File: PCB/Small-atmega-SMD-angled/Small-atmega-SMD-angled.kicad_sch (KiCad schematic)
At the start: 26 parts, among them J1 Daisy port out, J2 2-pin header, J3 ICSP_ISP6, J4 Daisy port in, K1 HYC77-TF09-200, U1 PC817C-S, U2 ATmega328P-AU, U3 SE5218, U4 TXB0104PWR, Y1 Resonator_GND2

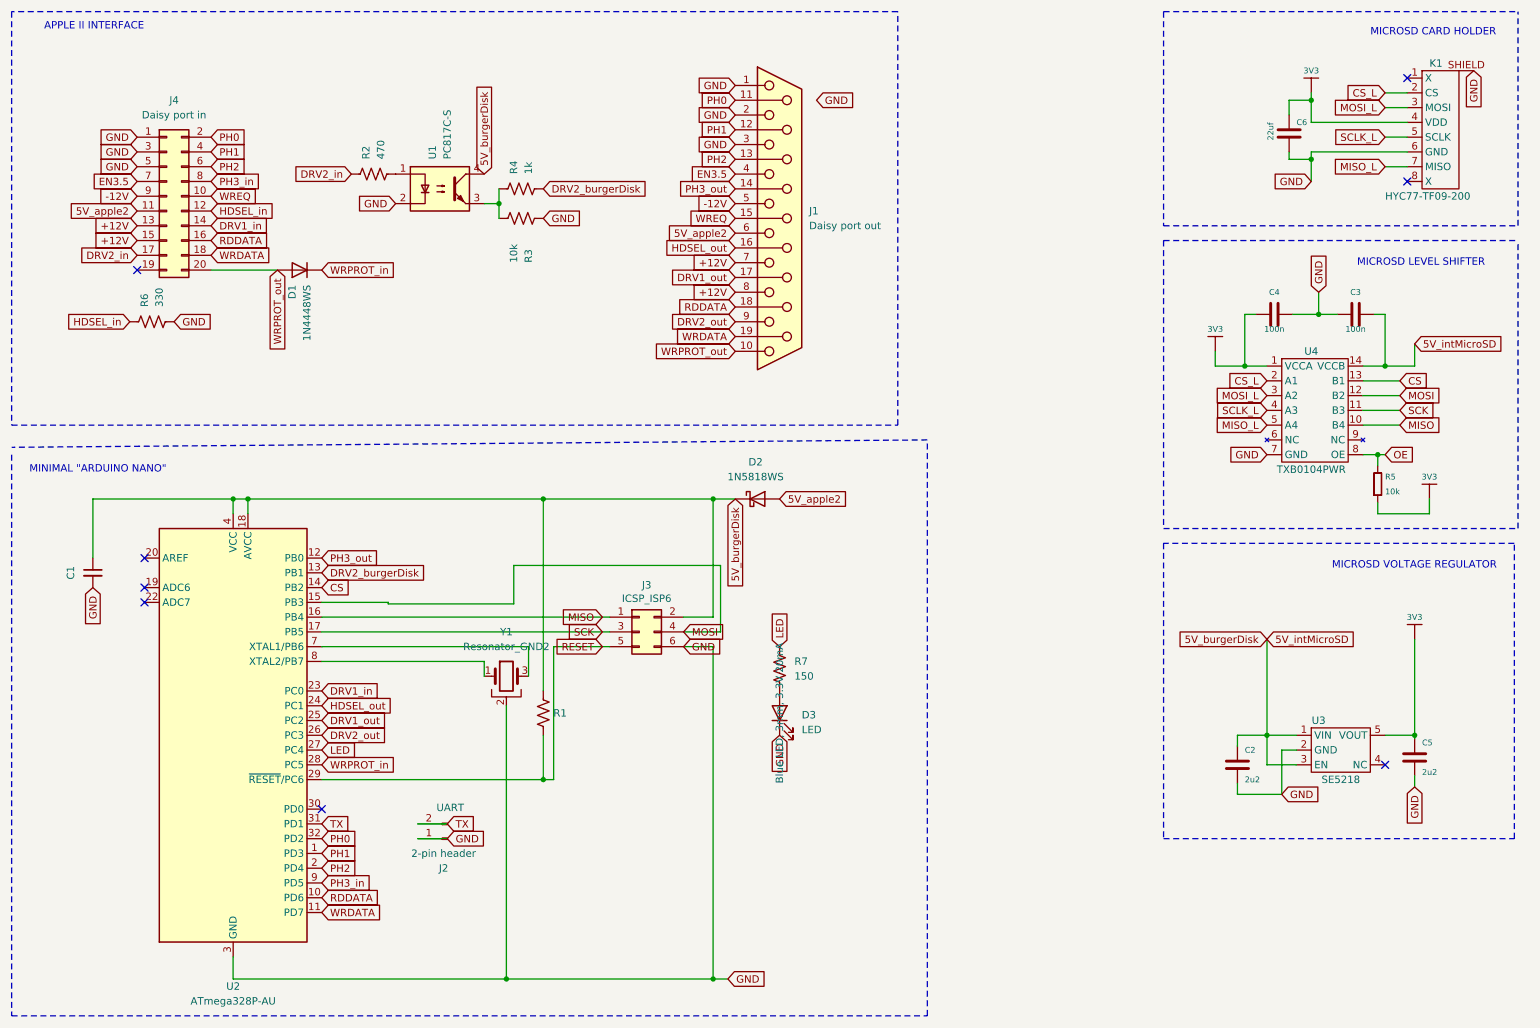
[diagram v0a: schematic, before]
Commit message: Add Mini variation with solder cups DB19F
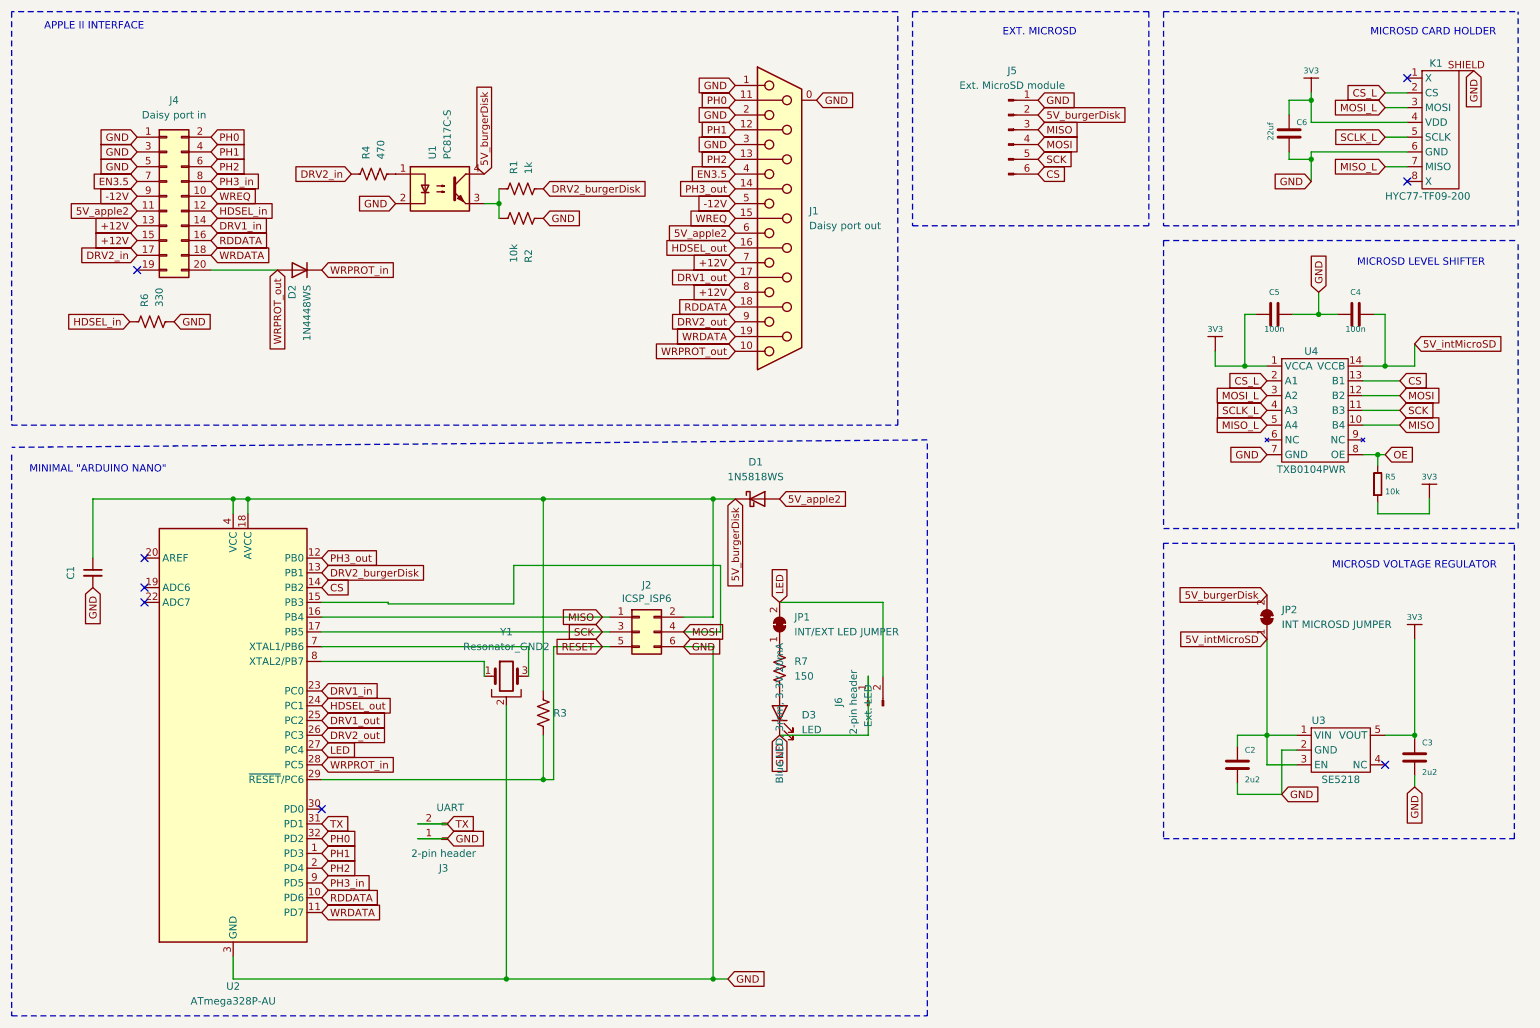
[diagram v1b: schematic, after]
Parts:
- added J5: Ext. MicroSD module, Connector_PinHeader_2.54mm:PinHeader_1x06_P2.54mm_Vertical, symbol Connector:Conn_01x06_Pin
- added J6: 2-pin header, Connector_PinHeader_2.54mm:PinHeader_1x02_P2.54mm_Vertical, symbol Connector:Conn_01x02_Pin
- added JP1: INT/EXT LED JUMPER, Jumper:SolderJumper-2_P1.3mm_Bridged_Pad1.0x1.5mm, symbol Jumper:SolderJumper_2_Bridged
- added JP2: INT MICROSD JUMPER, Jumper:SolderJumper-2_P1.3mm_Bridged_Pad1.0x1.5mm, symbol Jumper:SolderJumper_2_Bridged
- J1: footprint db19:DSUB-19_Female_EdgeMount_Pitch2.77mm -> DSUB-19-angled:DSUB-19_Female_Horizontal_MXS82009-8251-9246
- renumbered C5 to C3, C3 to C4, C4 to C5, D2 to D1, D1 to D2, J3 to J2, J2 to J3, R4 to R1, R3 to R2, R1 to R3, R2 to R4
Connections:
- net 5V_burgerDisk: now also J5.2 (Pin_2), JP2.2 (B); no longer C2.2, C4.2, U3.1 (VIN), U3.3 (EN), U4.14 (VCCB)
- net CS: now also J5.6 (Pin_6)
- net GND: now also J1.0, J5.1 (Pin_1), J6.1 (+5V)
- net LED: now also J6.2 (GND), JP1.2 (B); no longer R7.2
- net MISO: now also J5.3 (Pin_3)
- net MOSI: now also J5.4 (Pin_4)
- net SCK: now also J5.5 (Pin_5)
- new net: JP1.1 (A), R7.2
- new net 5V_intMicroSD: C2.2, C4.2, JP2.1 (A), U3.1 (VIN), U3.3 (EN), U4.14 (VCCB)
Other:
- note added: "EXT. MICROSD"
